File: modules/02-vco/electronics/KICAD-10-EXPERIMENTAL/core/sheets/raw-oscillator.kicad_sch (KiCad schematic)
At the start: 56 parts, among them Q1 BC847BS, Q2 MMBT3906, Q3 J111, Q4 MMBFJ111, Q5 MMBT5551, U1 TL072, U2 TL072, U3 LM311

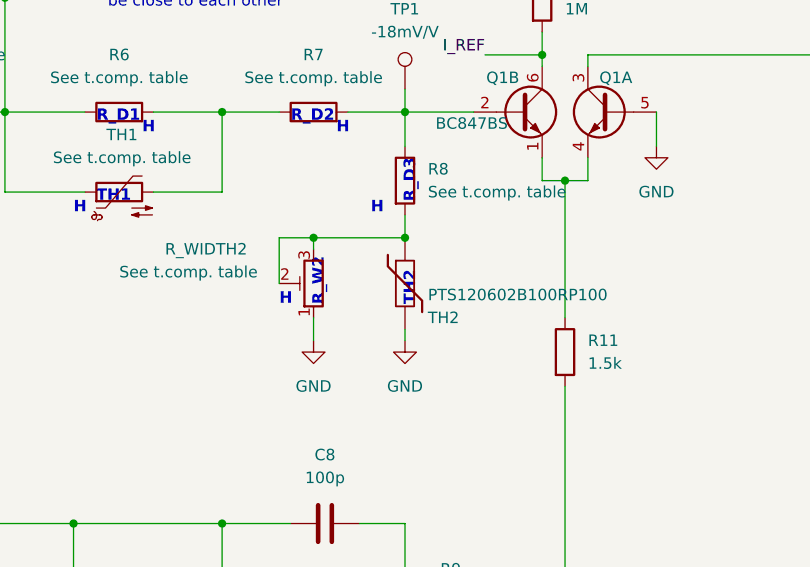
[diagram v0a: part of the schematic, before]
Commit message: Reverted VCO Core back to latest stable
- The latest working version of the VCO is this: (commit: https://github.com/shmoergh/moduleur/tree/b8f2f3887ee0ce40083da4d1238f04f5c6e473fa). Somewhere
between January 24 and May 24 the PCB got corrupted and it doesn't work properly. It could be the KiCAD 10 migration.
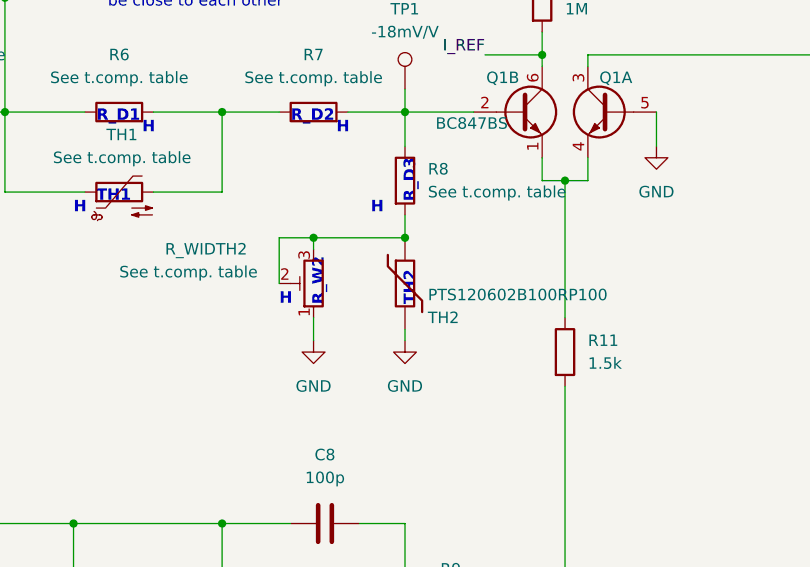
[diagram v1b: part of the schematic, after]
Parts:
- Q1: footprint Package_TO_SOT_SMD:SOT-363_SC-70-6 -> Shmoergh_Custom_Footprints:SOT-363_SC-70-6
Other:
- company: (none) -> Shmøergh
- title: (none) -> Moduleur VCO core
